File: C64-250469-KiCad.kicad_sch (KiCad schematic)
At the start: 137 parts, among them CN10 LED CONNECTOR, Q1 2SD313, Q2 2SC1815, Q3 2SC1815, Q5 2SC1384, U1 MOS6526, U19 COLOR_RAM_2114, U20 MOS8701, U22 INVERTER_OPENCOLLECTOR_7406, U23 INVERTER_SCHMITTTRIGGER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

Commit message: updated ibom with mouser pn. Cleaned up reference names for better grouping
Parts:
- C1, C84: Mouser (none) -> 81-RCER71H104K0K1H3B
- C19, C28, C29, C30, C34, C35, C37, C39, C40, C47, C48, C61, C69, C7, C79: value .1 -> 0,1u; Mouser (none) -> 81-RCER71H104K0K1H3B
- C2, C3, C4: value 470 -> 470pF; Mouser (none) -> 81-RCER71H471K0M1H3A
- C36: Mouser (none) -> 667-ECA-1CM470B
- C43: Mouser (none) -> 667-ECA-1CHG221B
- C44: Mouser (none) -> 667-ECA-1HHG2R2B
- C56: Mouser (none) -> 81-RCER71H103K0M1H3A
- C58: value 100u 16V -> 100u/16V; Mouser (none) -> 667-ECA-1CHG101B
- C59: Mouser (none) -> 667-ECE-A1EKS4R7B
- C6, C76, C90: Mouser (none) -> 81-RCER71H471K0M1H3A
- C63: Mouser (none) -> 594-MAL212535102E3
- C65: Mouser (none) -> 667-EEU-EB1E221SB
- C66: Mouser (none) -> 667-ECA-1VM471B
- C70, C71: Mouser (none) -> 81-RCER71H223K0K1H3B
- C74: Mouser (none) -> 81-RCER71H102K0M1H3A
- C77: Mouser (none) -> 667-ECA-1EM100B
- C80, C81: Mouser (none) -> 81-RCER71H222K0M1H3A
- C86, C87, C88: Mouser (none) -> 81-RCER71H221K0M1H3A
- C94: Mouser (none) -> 81-RCE5C1H151J0K1H3B
- CN1, CN10: Mouser (none) -> 855-M20-9992045
- CR1: Mouser (none) -> 78-1N5235B
- CR11, CR12, CR13, CR14, CR15, CR16, CR17, CR18, CR19, CR20, CR21, CR5: value ~ -> 1N914; Mouser (none) -> 78-1N4148
- CR2: Mouser (none) -> 583-BR34
- CR3, CR4: Mouser (none) -> 625-1N4001-E3/54
- CR6: Mouser (none) -> 78-1N5225B-TAP
- CR7: Mouser (none) -> 78-1N5240B
- CR9: Mouser (none) -> 78-1N4148
- DA1, DA2, DA3, DA4: Mouser (none) -> NU
- EM1, EM2, EM3, EM4, EM5, EM6, EM7, EM8, EM9: Mouser (none) -> 81-DSS1NB32A271Q91A
- R2: value 20 -> SeeTable
- U10, U11: value ~ -> 4164 DRAM
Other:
- note added: "20"

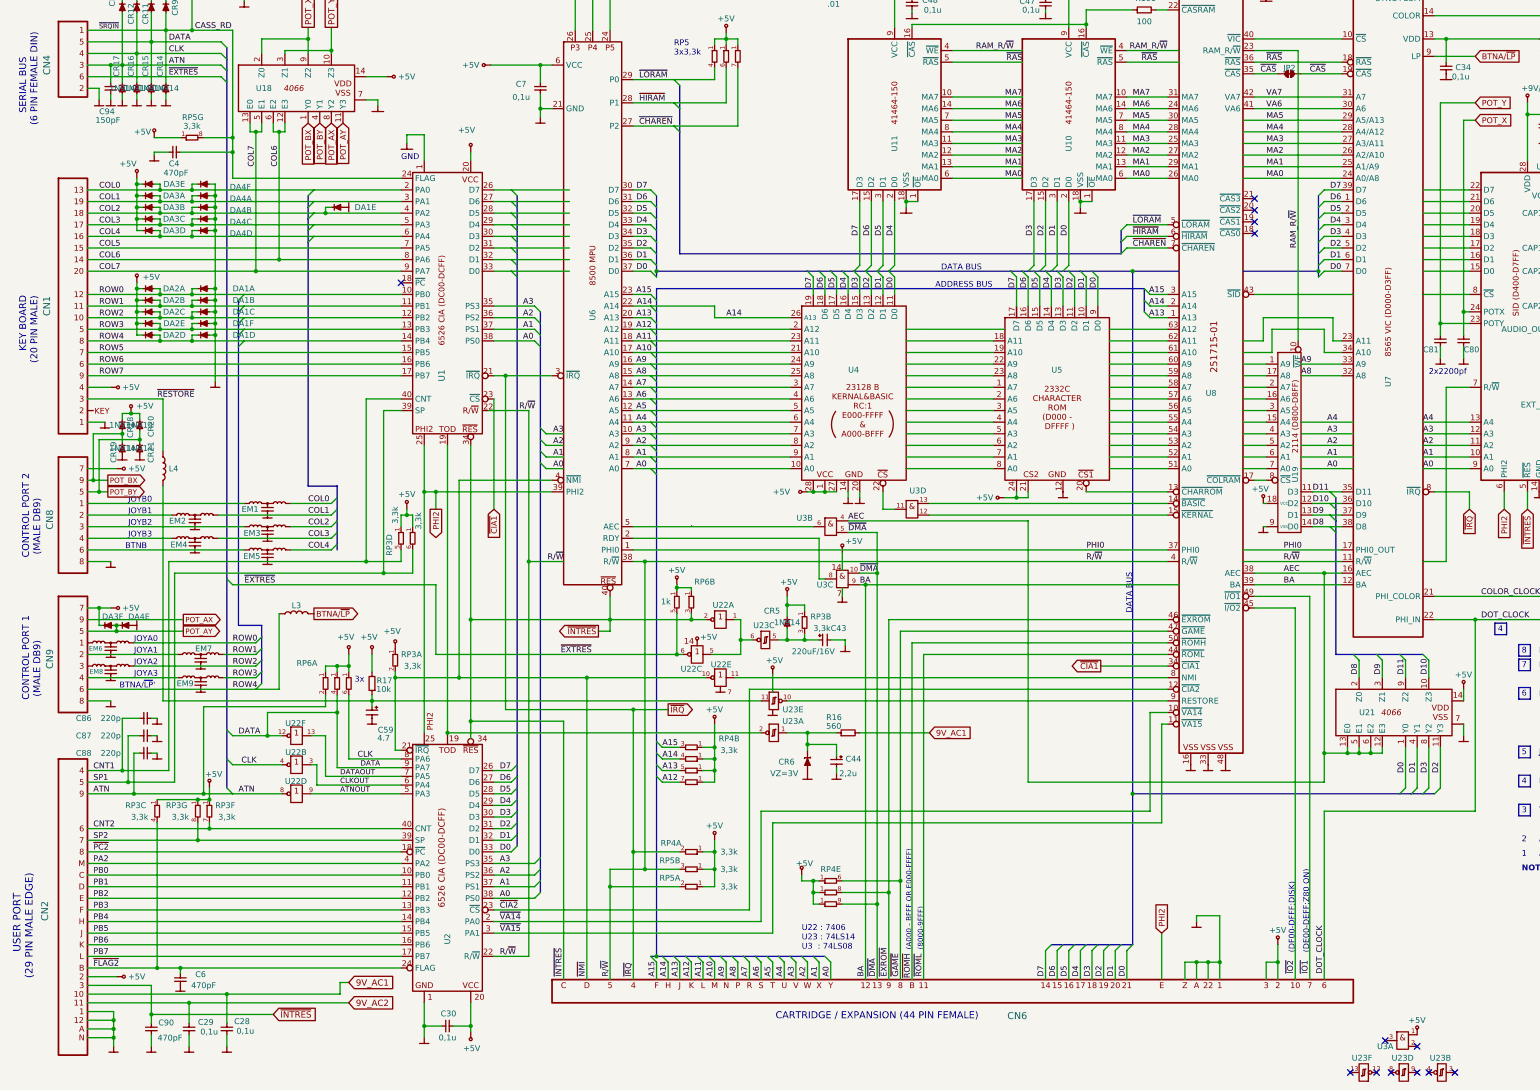
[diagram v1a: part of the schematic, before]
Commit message: Updated digi-key order numbers, about 50 percent of them done. new ibom.html
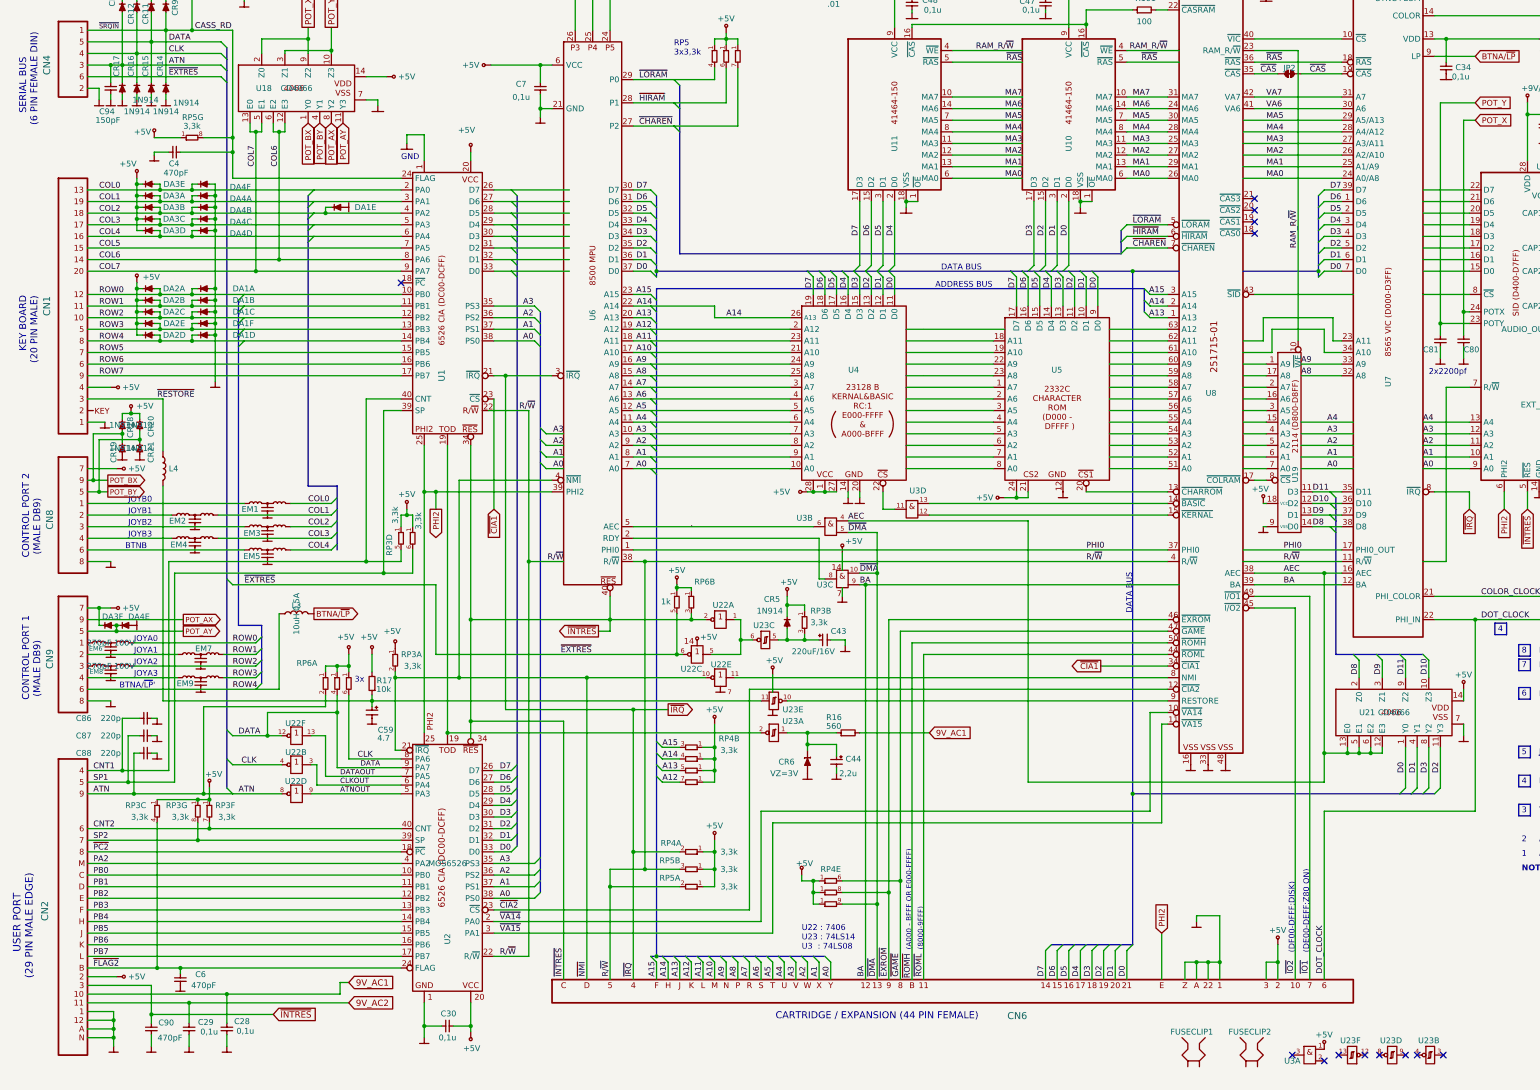
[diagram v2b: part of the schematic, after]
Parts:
- added FUSECLIP1, FUSECLIP2: ~, symbol c64c-symbol-library:FUSECLIP
- C1, C19, C28, C29, C30, C34, C35, C37, C39, C40, C47, C48, C61, C69, C7, C79, C84: Digi-Key (none) -> 445-173588-1-ND
- C2, C3, C4, C6, C76, C90: Digi-Key (none) -> 445-173500-1-ND
- C36: Digi-Key (none) -> P19514CT-ND
- C43: Digi-Key (none) -> 10-ECA-1CHG221BCT-ND
- C44: Digi-Key (none) -> P15752CT-ND
- C56: Digi-Key (none) -> 490-7513-1-ND
- C58: Digi-Key (none) -> 10-ECA-1CHG101BCT-ND
- C59: Digi-Key (none) -> 10-ECE-A1VKS4R7BCT-ND
- C63: Digi-Key (none) -> 1572-1063-ND
- C65: Digi-Key (none) -> 10-EEU-EB1E221SBCT-ND
- C66: Digi-Key (none) -> P15391TB-ND
- C70, C71: Digi-Key (none) -> 445-173593-1-ND
- C74: Digi-Key (none) -> 490-7511-1-ND
- C77: Digi-Key (none) -> P19522CT-ND
- C80, C81: Digi-Key (none) -> 445-173592-1-ND
- C86, C87, C88: Digi-Key (none) -> 445-180773-1-ND
- C94: Digi-Key (none) -> 445-173479-1-ND
- EM1, EM2, EM3, EM4, EM5, EM6, EM7, EM8, EM9: value ~ -> 270pF 100V
- F1: Mouser (none) -> 504-BK/AGC-1-1/2-R
- FB1: value FERRITE_BEAD -> FERRITE_BEAD_TWO_TURN; Mouser (none) -> 81-BL02RN2R1M2B
- FB2, FB3, FB4: Mouser (none) -> 81-BL01RN1A1F1J
- L1: Digi-Key (none) -> ?
- L2: Digi-Key (none) -> M10140-ND; Mouser (none) -> 652-78F2R2J-RC
- L3, L4: value ~ -> 10uH 0.5A; Digi-Key (none) -> 399-SBT-0210-ND; Mouser (none) -> 80-SBT-0210
- R1: Digi-Key (none) -> 13-MFR50SFRF52-470RCT-ND
- R100: Digi-Key (none) -> 13-MFR-25FTE52-1K8CT-ND
- R101: Digi-Key (none) -> 100XBK-ND
- R12, R3, R8: Digi-Key (none) -> 13-MFR-25FTF52-1KCT-ND
- R14: Digi-Key (none) -> 13-MFR-25FRF52-100KCT-ND
- R16: Digi-Key (none) -> MFR-25FBF52-560R-ND
- R17, R9: Digi-Key (none) -> 13-MFR-25FRF52-10KCT-ND
- R19: Digi-Key (none) -> 13-MFR50SFTE52-10RCT-ND
- R2: Digi-Key (none) -> Not Used
- R5: Digi-Key (none) -> MFR-25FBF52-390R-ND
- U18, U21: value ~ -> CD4066
- U2: value ~ -> MOS6526
- U22: Mouser (none) -> 595-SN7406NE4
- U23: Mouser (none) -> 595-SN74HCT14N
- U3: Mouser (none) -> 595-SN74HCT08N
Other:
- moved on the sheet: U23B, U23D, U23F, U3A

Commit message: updated ibom
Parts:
- added SKT1, SKT2, SKT6, SKT7: DIP40, symbol c64c-symbol-library:SOCKET
- added SKT10, SKT11, SKT19: DIP18, symbol c64c-symbol-library:SOCKET
- added SKT18, SKT21, SKT22, SKT23, SKT3: DIP14, symbol c64c-symbol-library:SOCKET
- added SKT20: DIP16, symbol c64c-symbol-library:SOCKET
- added SKT4, SKT9: DIP28, symbol c64c-symbol-library:SOCKET
- added SKT5: DIP24, symbol c64c-symbol-library:SOCKET
- added SKT8: DIP64, symbol c64c-symbol-library:SOCKET
- CN1, CN10: Digi-Key (none) -> 952-3306-ND
- CN2, CN3: now left out of the parts list
- CN8, CN9: Digi-Key (none) -> 625-009-262-033-ND
- CR1: Digi-Key (none) -> 1N5235BVSCT-ND
- CR11, CR12, CR13, CR14, CR15, CR16, CR17, CR18, CR19, CR20, CR21, CR5, CR9: Digi-Key (none) -> 1N914FS-ND
- CR2: Digi-Key (none) -> PB64-BPMS-ND
- CR3, CR4: Digi-Key (none) -> 1N4001-E3/54GICT-ND
- CR6: Digi-Key (none) -> 112-1N5225B-TAPTB-ND
- CR7: Digi-Key (none) -> 1N5240BVSCT-ND
- CT1: Digi-Key (none) -> 2447-GKG30015-ND
- DA1, DA2, DA3, DA4: Digi-Key (none) -> NU
- EM1, EM2, EM3, EM4, EM5, EM6, EM7, EM8, EM9: Digi-Key (none) -> DSS1NB32A271Q91A
- F1: Digi-Key (none) -> 283-2623-ND
- FB1: Digi-Key (none) -> 535-12434-ND
- FB2, FB3, FB4: Digi-Key (none) -> 240-2513-1-ND
- FUSECLIP1, FUSECLIP2: Digi-Key (none) -> 283-2601-ND
- Q1: Digi-Key (none) -> TIP29AGOS-ND
- Q2, Q3: Digi-Key (none) -> 1514-2SC1815PBFREE-ND
- Q5: Digi-Key (none) -> KSD1616AGTATB-ND
- RP3, RP5: Digi-Key (none) -> 4608X-1-332LF-ND
- RP4: Digi-Key (none) -> 4609X-101-332LF-ND
- RP6: Digi-Key (none) -> 4606X-1-102LF-ND
- SW1: Digi-Key (none) -> 360-4016-ND
- U18, U21: Digi-Key (none) -> 296-2061-5-ND
- U22: value INVERTER_OPENCOLLECTOR_7406 -> 74LS06; Digi-Key (none) -> 296-15069-5-ND
- U23: value INVERTER_SCHMITTTRIGGER -> 74LS14; Digi-Key (none) -> 296-1643-5-ND
- U3: value 74LS08_AND -> 74LS08; Digi-Key (none) -> 296-1633-5-ND
- Y1: value Crystal -> 17.734475 MHz; Digi-Key (none) -> 887-2042-ND
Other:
- moved on the sheet: FUSECLIP1, FUSECLIP2, U23B, U23D, U23F, U3A
